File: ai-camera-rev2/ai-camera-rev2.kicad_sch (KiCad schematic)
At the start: 174 parts, among them J1 Conn-01x02_P2mm_NONAME_JST-PH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, J2 TYPE-C-31-M-12, J3 MAXLAB, J4 Conn-02x10_P2.54mm_B-2100S20P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, J5 Conn-01x02_P1.25mm_10114829-1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, J6 Conn_01x24_FFC_0.5mm_AFC01-S2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, Q1 2N7002, Q2 2N7002, Q3 AO3401A, Q4 AO3401A, Q5 2N7002, Q6 AO3401A, Q7 2N7002, Q8 AO3401A, Q9 2N7002, SW1 SW_PB_90deg_K2-1102AQ-H4CW-01, SW2 SW_PB_TS-1187A-B-A-B, SW3 SW_PB_TS-1187A-B-A-B, SW4 SW_PB_90deg_K2-1102AQ-H4CW-01, U1 TP4057-42-SOT26-R, U10 ESP32-S3-WROOM-1-N16R8, U11 MT9284-28J, U12 LTR-303ALS-01, U2 XC6206-2.8V, U3 PCF85063AT_SO8, U4 SOT-23-6_SN74LVC1G373DBVR_TI, U5 SY8089AAAC, U6 PIR_AS312, U7 XC6206-2.8V, U8 RT9166-12GVL, U9 AP1511B, Y1 32.768kHz_Q13FC1350000400

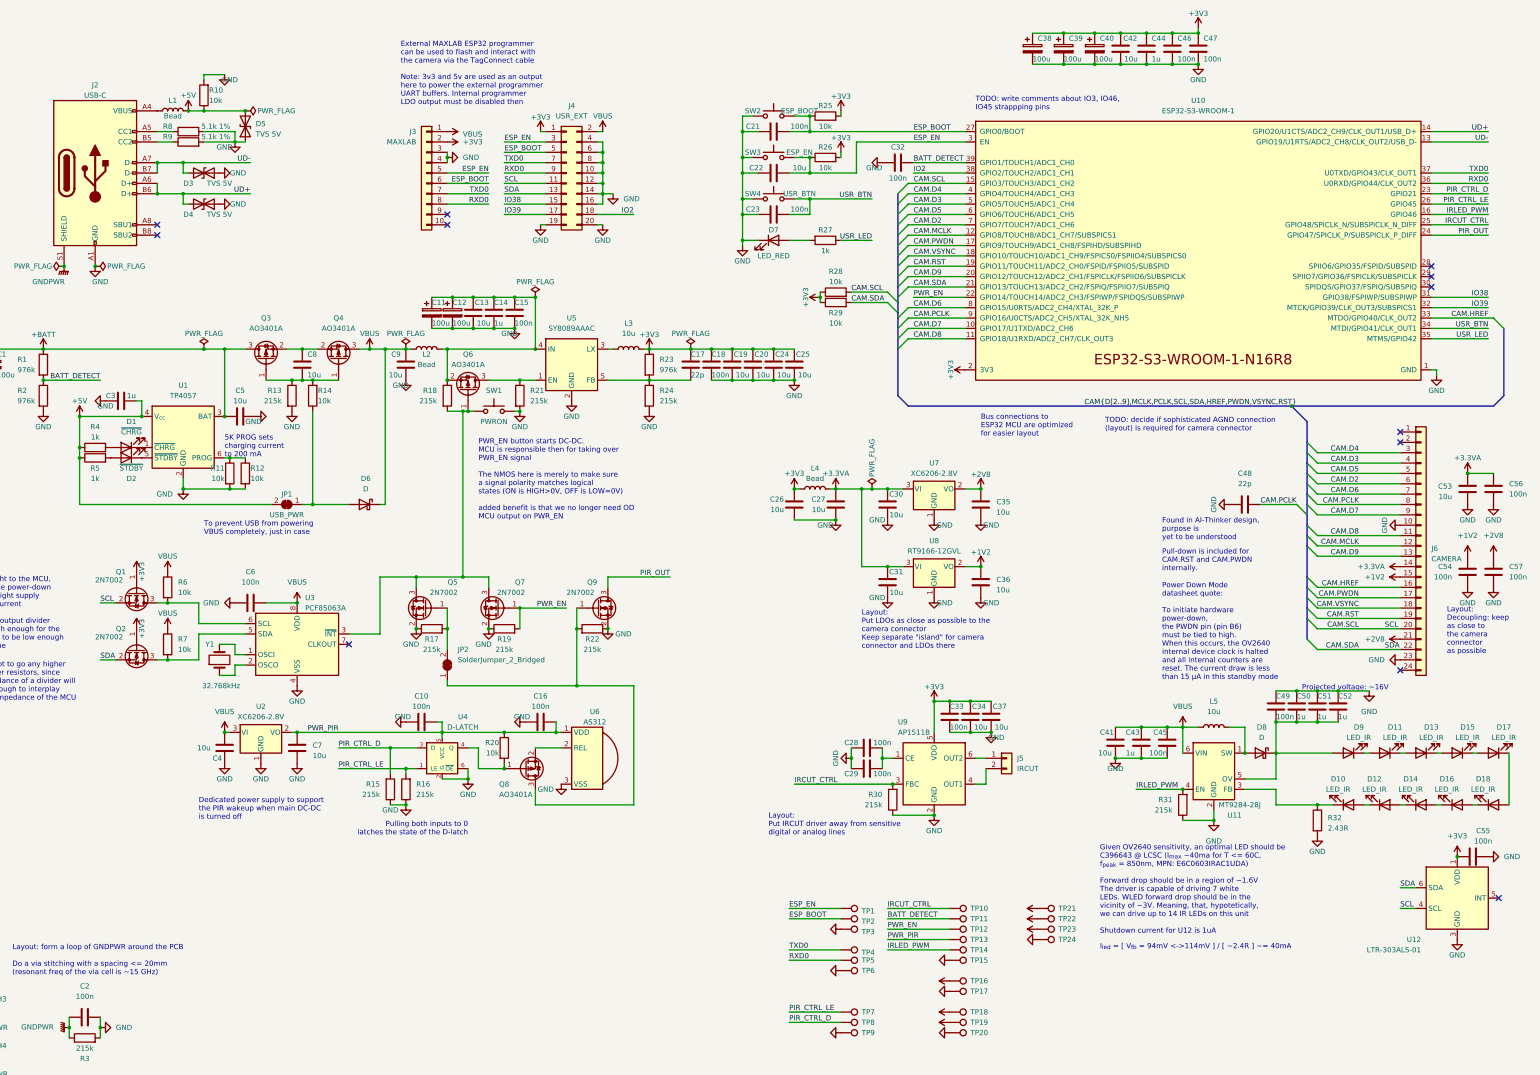
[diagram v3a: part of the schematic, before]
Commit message: EAC-49: update silkscreen and use single capacitor for all decoupling
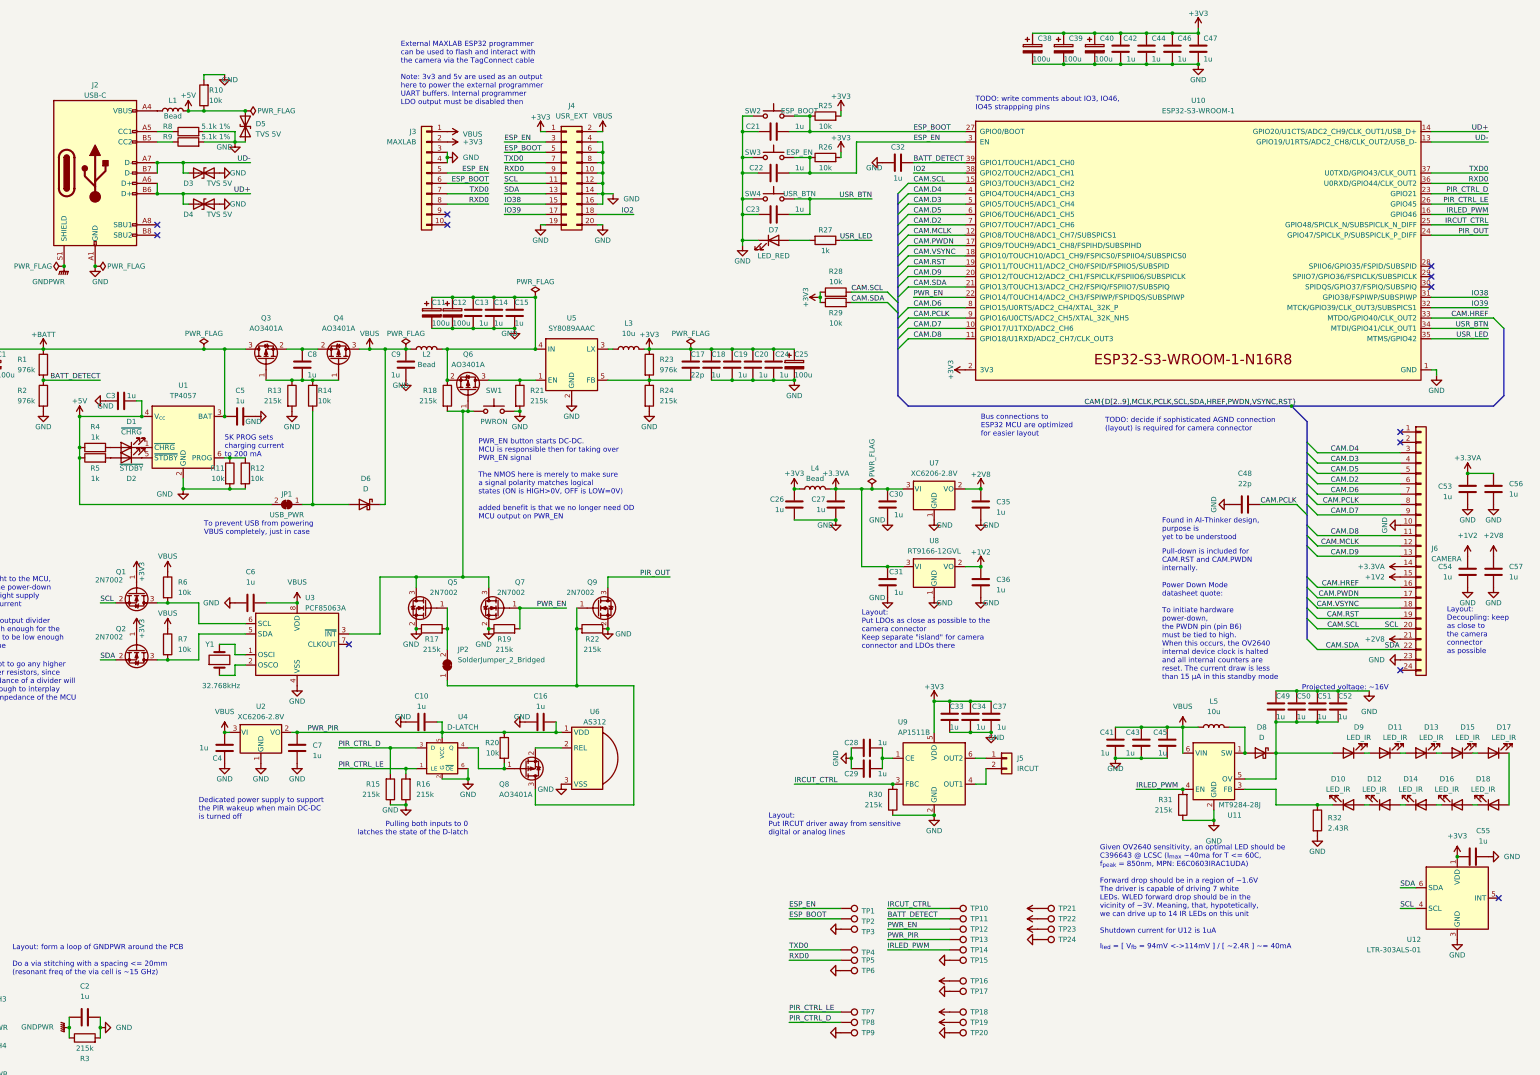
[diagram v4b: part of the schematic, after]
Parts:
- removed C25: 10u_0603_CL10A106KP8NNNC, Capacitor_SMD:C_0603_1608Metric, symbol 00-kiml-capacitors-smd:10u_0603_CL10A106KP8NNNC
- added C25: 100u_CASE-B-3528_TAJB107K006RNJ, 00-kiml-capacitor-tantalum:CP_EIA-3528-15_AVX-H, symbol 00-kiml-capacitors-smd:100u_CASE-B-3528_TAJB107K006RNJ
- C10, C15, C16, C18, C2, C21, C23, C28, C29, C32, C33, C45, C46, C47, C49, C54, C55, C56, C57, C6: value 100n_0402_CL05B104KB54PNC -> 10u_0402_CL05A105KA5NQNC; symbol 00-kiml-capacitors-smd:100n_0402_CL05B104KB54PNC -> 00-kiml-capacitors-smd:1u_0402_CL05A105KA5NQNC; LNK1 https://jlcpcb.com/partdetail/291005-CL05B104KB54PNC/C307331 -> https://jlcpcb.com/partdetail/53938-CL05A105KA5NQNC/C52923; MPN CL05B104KB54PNC -> CL05A105KA5NQNC; Rating 50V -> 25V; SNB1 Basic part -> Basic Part; SPN1 C307331 -> C52923; UserValue 100n -> 1u
- C13, C19, C20, C22, C24, C26, C27, C30, C31, C34, C35, C36, C37, C4, C41, C42, C5, C53, C7, C8, C9: value 10u_0603_CL10A106KP8NNNC -> 10u_0402_CL05A105KA5NQNC; footprint Capacitor_SMD:C_0603_1608Metric -> Capacitor_SMD:C_0402_1005Metric; symbol 00-kiml-capacitors-smd:10u_0603_CL10A106KP8NNNC -> 00-kiml-capacitors-smd:1u_0402_CL05A105KA5NQNC; LNK1 https://jlcpcb.com/partdetail/20411-CL10A106KP8NNNC/C19702 -> https://jlcpcb.com/partdetail/53938-CL05A105KA5NQNC/C52923; MPN CL10A106KP8NNNC -> CL05A105KA5NQNC; Rating 10V -> 25V; SNB1 Basic part -> Basic Part; SPN1 C19702 -> C52923; UserValue 10u -> 1u
- C14, C3, C43, C44, C50, C51, C52: value 1u_0603_CL10A105KB8NNNC -> 10u_0402_CL05A105KA5NQNC; footprint Capacitor_SMD:C_0603_1608Metric -> Capacitor_SMD:C_0402_1005Metric; symbol 00-kiml-capacitors-smd:1u_0603_CL10A105KB8NNNC -> 00-kiml-capacitors-smd:1u_0402_CL05A105KA5NQNC; LNK1 https://jlcpcb.com/partdetail/16531-CL10A105KB8NNNC/C15849 -> https://jlcpcb.com/partdetail/53938-CL05A105KA5NQNC/C52923; MPN CL10A105KB8NNNC -> CL05A105KA5NQNC; Rating 50V -> 25V; SPN1 C15849 -> C52923
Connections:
- net +3V3: now also C25.1
- net GND: now also C25.2

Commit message: EAC-49: add power-on detection in case of user button press
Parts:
- added Q9: 2N7002, Package_TO_SOT_SMD:SOT-23, symbol 00-kiml-transistor-fet:2N7002
- added R22: 215k_0402_0402WGD2153TCE, Resistor_SMD:R_0402_1005Metric, symbol 00-kiml-resistors-smd:215k_0402_0402WGD2153TCE
- JP2: value SolderJumper_2_Bridged -> PIR
- renumbered Q9 to Q10, R22 to R25, R25 to R26, R26 to R27, R27 to R28, R28 to R29, R29 to R30, R30 to R31, R31 to R32, R32 to R33
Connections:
- net GND: now also J4.18 (Pin_18), Q9.2 (S), R22.1; no longer SW1.2
- net VBUS: now also SW1.1
- net at Q5.3 (D), Q6.1 (G), Q7.3 (D)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: now also Q9.3 (D); no longer SW1.1
- net IO2 renamed PWRON_DET
- net PWRON_DET: now also SW1.2, Q9.1 (G), R22.2; no longer J4.18 (Pin_18)
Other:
- note added: "PWR_ON button starts DC-DC. MCU is responsible then for taking over PWR_EN signal The NMOS here is merely to make sure a signal polarity matches logical states (ON is HIGH>0V, OFF is LOW=0V) added benefit is that we no longer need OD MCU output on PWR_EN"
- note removed: "PWR_EN button starts DC-DC. MCU is responsible then for taking over PWR_EN signal The NMOS here is merely to make sure a signal polarity matches logical states (ON is HIGH>0V, OFF is LOW=0V) added benefit is that we no longer need OD MCU output on PWR_EN"
- moved on the sheet: JP2, Q10, Q5, Q7, R17, R19, R25, SW1

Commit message: EAC-49: PWR_PIR instead of VBUS for PWRON button trigger
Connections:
- net PWR_PIR: now also SW1.1
- net VBUS: no longer SW1.1
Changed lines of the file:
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@@
     (stroke (width 0) (type default))
   )
+  (wire (pts (xy 176.53 148.59) (xy 176.53 154.94))
+    (stroke (width 0) (type default))
+  )
   (wire (pts (xy 267.97 154.94) (xy 271.78 154.94))
     (stroke (width 0) (type default))
@@
     (effects (font (size 1.27 1.27)) (justify left bottom))
   )
+  (label "PWR_PIR" (at 176.53 148.59 270) (fields_autoplaced)
+    (effects (font (size 1.27 1.27)) (justify right bottom))
+  )
   (label "PWRON_DET" (at 187.96 165.1 180) (fields_autoplaced)
     (effects (font (size 1.27 1.27)) (justify right bottom))
@@
         )
       )
-    )
-  )
-  (symbol (lib_id "power:VBUS") (at 176.53 154.94 0) (unit 1)
-    (in_bom yes) (on_board yes) (dnp no) (fields_autoplaced)
-    (property "Reference" "#PWR052" (at 176.53 158.75 0)
-      (effects (font (size 1.27 1.27)) hide)
-    )
-    (property "Value" "VBUS" (at 176.53 151.13 0)
-      (effects (font (size 1.27 1.27)))
-    )
-    (property "Footprint" "" (at 176.53 154.94 0)
-      (effects (font (size 1.27 1.27)) hide)
-    )
-    (property "Datasheet" "" (at 176.53 154.94 0)
-      (effects (font (size 1.27 1.27)) hide)
-    )
-    (pin "1")
-    (instances
-      (project "ai-camera-rev2"
-        (path "/9e3de00a-ea10-4aff-9cb7-2823d660607b"
-          (reference "#PWR052") (unit 1)
-        )
-      )
